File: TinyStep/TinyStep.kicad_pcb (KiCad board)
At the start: 2 copper layers, 17.8 x 25.4 mm, 2 parts, among them U1 ATtiny204-SS

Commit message: this might work
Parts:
- added A1: Pololu_Breakout_A4988, Module:Pololu_Breakout-16_15.2x20.3mm, F.Cu at (57.1, 35.5)
- added C2: 100uF 50V, Capacitor_THT:CP_Radial_D8.0mm_P3.50mm, F.Cu at (40.0, 39.6)
- added J1: Conn_01x03_Pin, Connector_PinHeader_2.54mm:PinHeader_1x03_P2.54mm_Vertical, F.Cu at (40.0, 52.1)
- added J2: Conn_01x04_Pin, Connector_JST:JST_XH_S4B-XH-A_1x04_P2.50mm_Horizontal, F.Cu at (52.0, 29.2)
- added J3: Conn_01x02_Pin, Connector_PinHeader_2.54mm:PinHeader_1x02_P2.54mm_Vertical, F.Cu at (57.8, 51.4)
- added J4: Conn_01x02_Pin, Connector_PinHeader_2.54mm:PinHeader_1x02_P2.54mm_Vertical, F.Cu at (57.8, 54.0)
- added J5: Conn_01x02_Pin, Connector_PinHeader_2.54mm:PinHeader_1x02_P2.54mm_Vertical, F.Cu at (57.8, 56.5)
- added J6: Conn_01x02_Pin, Connector_PinHeader_2.54mm:PinHeader_1x02_P2.54mm_Vertical, F.Cu at (57.8, 59.0)
- added J7: Barrel_Jack_Switch, Connector_BarrelJack:BarrelJack_Wuerth_6941xx301002, F.Cu at (47.9, 61.0)
- added R1: 10k, Resistor_SMD:R_0805_2012Metric_Pad1.20x1.40mm_HandSolder, B.Cu at (46.4, 45.1)
- added R2: 10k, Resistor_SMD:R_0805_2012Metric_Pad1.20x1.40mm_HandSolder, B.Cu at (44.5, 45.1)
- added R3: 10k, Resistor_SMD:R_0805_2012Metric_Pad1.20x1.40mm_HandSolder, B.Cu at (42.5, 45.1)
- added R4: 10k, Resistor_SMD:R_0805_2012Metric_Pad1.20x1.40mm_HandSolder, B.Cu at (51.4, 50.8)
- added R5: 10k, Resistor_SMD:R_0805_2012Metric_Pad1.20x1.40mm_HandSolder, B.Cu at (51.4, 52.7)
- added R6: 10k, Resistor_SMD:R_0805_2012Metric_Pad1.20x1.40mm_HandSolder, B.Cu at (51.4, 54.6)
- added R7: 10k, Resistor_SMD:R_0805_2012Metric_Pad1.20x1.40mm_HandSolder, B.Cu at (51.4, 56.5)
- added SW1: SW_DIP_x03, Button_Switch_SMD:SW_DIP_SPSTx03_Slide_Omron_A6S-310x_W8.9mm_P2.54mm, F.Cu at (47.6, 54.6)
- C1: value C -> 100n; footprint Capacitor_THT:C_Disc_D5.0mm_W2.5mm_P5.00mm -> Capacitor_SMD:C_0805_2012Metric_Pad1.18x1.45mm_HandSolder; moved to B.Cu
- U1: footprint BREAKOUT:DIP-16_SOIC_BREAKOUT -> Package_SO:SOIC-14_3.9x8.7mm_P1.27mm; moved to B.Cu
- moved U1 37.4 mm to (54.0, 42.5), turned to -90 degrees
- moved C1 29.1 mm to (48.3, 41.9), turned to 90 degrees
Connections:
- net Net-(U1-GND) renamed GND
- U1 pad 10: unconnected-(U1-~{RESET}/PA0-Pad10) -> UPDI
- U1 pad 11: unconnected-(U1-PA1-Pad11) -> A1_DI
- U1 pad 12: unconnected-(U1-PA2-Pad12) -> A1_ST
- U1 pad 13: unconnected-(U1-PA3-Pad13) -> A1_EN
- U1 pad 2: unconnected-(U1-PA4-Pad2) -> BTN0
- U1 pad 3: unconnected-(U1-PA5-Pad3) -> BTN1
- U1 pad 4: unconnected-(U1-PA6-Pad4) -> BTN3
- U1 pad 5: unconnected-(U1-PA7-Pad5) -> BTN2
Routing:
- net VCC: track 3.89 -> 55.4 mm
- net +12V: track 0.00 -> 36.9 mm
- net BTN3: track 0.00 -> 30.0 mm
- net UPDI: track 0.00 -> 28.1 mm, vias 0 -> 2
- net BTN2: track 0.00 -> 23.3 mm
- net BTN1: track 0.00 -> 21.3 mm, vias 0 -> 1
- net BTN0: track 0.00 -> 18.4 mm, vias 0 -> 1
- net A1_EN: track 0.00 -> 16.3 mm, vias 0 -> 1
- net Net-(A1-MS3): track 0.00 -> 14.8 mm
- net GND: track 10.4 -> 0.00 mm
- net Net-(A1-MS2): track 0.00 -> 10.3 mm
- net Net-(A1-MS1): track 0.00 -> 6.77 mm
- net Net-(A1-1B): track 0.00 -> 6.40 mm
- net Net-(A1-1A): track 0.00 -> 6.38 mm
- net Net-(A1-2A): track 0.00 -> 6.37 mm
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- added copper zone on B.Cu, net GND
- added copper zone on F.Cu, net GND
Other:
- board size 17.8 x 25.4 mm -> 26 x 54 mm
- board text added: "1 0"
- board text added: "B2 A2 A1 B1"
- board text added: "GND VCC UPDI"
- board text added: "MS1 MS2 MS3"

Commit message: v0.1
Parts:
- removed A1: Pololu_Breakout_A4988, Module:Pololu_Breakout-16_15.2x20.3mm
- removed the J3 at (57.8, 51.4)
- removed J6: Conn_01x02_Pin, Connector_PinHeader_2.54mm:PinHeader_1x02_P2.54mm_Vertical
- removed R5, R6, R7: 10k, Resistor_SMD:R_0805_2012Metric_Pad1.20x1.40mm_HandSolder
- removed SW1: SW_DIP_x03, Button_Switch_SMD:SW_DIP_SPSTx03_Slide_Omron_A6S-310x_W8.9mm_P2.54mm
- added A2: ~, Module_TMC2209_BTT:TMC2209_BTT, F.Cu at (52.2, 38.7)
- added C3: 10uF, Capacitor_SMD:C_0805_2012Metric_Pad1.18x1.45mm_HandSolder, B.Cu at (47.5, 41.2)
- added C4: 100nF, Capacitor_SMD:C_0805_2012Metric_Pad1.18x1.45mm_HandSolder, B.Cu at (49.7, 36.3)
- added C5: 22uF, Capacitor_SMD:C_0805_2012Metric_Pad1.18x1.45mm_HandSolder, B.Cu at (52.4, 40.3)
- added C6: 22uF, Capacitor_SMD:C_0805_2012Metric_Pad1.18x1.45mm_HandSolder, B.Cu at (50.4, 40.3)
- added JP1: SolderJumper_3_Bridged12, Jumper:SolderJumper-3_P1.3mm_Bridged12_RoundedPad1.0x1.5mm_NumberLabels, F.Cu at (53.6, 48.9)
- added JP2: SolderJumper_2_Open, Jumper:SolderJumper-2_P1.3mm_Open_RoundedPad1.0x1.5mm, F.Cu at (53.1, 51.8)
- added JP3: SolderJumper_2_Open, Jumper:SolderJumper-2_P1.3mm_Open_RoundedPad1.0x1.5mm, F.Cu at (50.5, 51.8)
- added JP4: SolderJumper_2_Open, Jumper:SolderJumper-2_P1.3mm_Open_RoundedPad1.0x1.5mm, F.Cu at (48.0, 51.8)
- added L1: 4.7uH, Inductor_SMD:L_0805_2012Metric_Pad1.15x1.40mm_HandSolder, B.Cu at (51.7, 36.3)
- added U2: AP63205WU, Package_TO_SOT_SMD:TSOT-23-6, B.Cu at (46.9, 38.0)
- C1: value 100n -> 100nF
- C2: value 100uF 50V -> 47uF 50V; footprint Capacitor_THT:CP_Radial_D8.0mm_P3.50mm -> Capacitor_SMD:CP_Elec_6.3x7.7
- J4: value Conn_01x02_Pin -> Conn_02x05_Odd_Even; footprint Connector_PinHeader_2.54mm:PinHeader_1x02_P2.54mm_Vertical -> Connector_PinHeader_2.54mm:PinHeader_2x05_P2.54mm_Vertical
- J5: value Conn_01x02_Pin -> Conn_02x02_Odd_Even; footprint Connector_PinHeader_2.54mm:PinHeader_1x02_P2.54mm_Vertical -> Connector_PinHeader_2.54mm:PinHeader_2x02_P2.54mm_Vertical
- R4: value 10k -> 1k
- moved R3 16.8 mm to (58.6, 40.3)
- moved J5 15.4 mm to (43.0, 60.8), turned to 0 degrees
- moved R2 13.0 mm to (56.6, 40.3)
- moved U1 11.1 mm to (50.7, 53.1), turned to 180 degrees
- moved C2 9.94 mm to (49.7, 37.6), turned to 0 degrees
- moved R1 9.44 mm to (54.5, 40.3)
- moved R4 7.95 mm to (57.7, 55.7), turned to 90 degrees
- moved J1 6.62 mm to (44.2, 57.2), turned to 180 degrees
- moved C1 6.10 mm to (50.7, 47.5), turned to 180 degrees
- moved J3 4.50 mm to (52.4, 60.4)
- moved J2 4.30 mm to (56.0, 27.7)
- moved J4 3.91 mm to (60.5, 51.2), turned to 0 degrees
- renumbered J7 to J3
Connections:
- C1 pad 1: GND -> VCC
- C1 pad 2: VCC -> GND
- J4 pad 1: BTN1 -> BTN0
- J4 pad 2: Net-(J4-Pin_2) -> GND
- J5 pad 1: BTN2 -> VCC
- J5 pad 2: Net-(J5-Pin_2) -> GND
- R3 pad 2: Net-(A1-MS1) -> A1_MS3_SW
- R4 pad 1: Net-(J3-Pin_2) -> /USART_Tx
- R4 pad 2: VCC -> A1_MS3_UART
- U1 pad 11: A1_DI -> BTN2
- U1 pad 12: A1_ST -> A1_DIAG
- U1 pad 2: BTN0 -> A1_ST
- U1 pad 3: BTN1 -> A1_DI
- U1 pad 4: BTN3 -> BTN0
- U1 pad 5: BTN2 -> BTN1
- U1 pad 6: unconnected-(U1-PB3-Pad6) -> A1_MS3_UART
- U1 pad 7: unconnected-(U1-PB2-Pad7) -> /USART_Tx
- U1 pad 8: unconnected-(U1-PB1-Pad8) -> BTN4
- U1 pad 9: unconnected-(U1-PB0-Pad9) -> BTN3
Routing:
- net +12V: track 36.9 -> 62.4 mm
- net UPDI: track 28.1 -> 5.84 mm, vias 2 -> 0
- net A1_MS3_SW: track 0.00 -> 22.3 mm, vias 0 -> 1
- net VCC: track 55.4 -> 73.3 mm, vias 0 -> 2
- net A1_DIAG: track 0.00 -> 16.6 mm
- net BTN3: track 30.0 -> 14.3 mm
- net BTN4: track 0.00 -> 14.1 mm
- net A1_MS3_UART: track 0.00 -> 13.6 mm, vias 0 -> 1
- net BTN1: track 21.3 -> 8.48 mm, vias 1 -> 0
- net BTN0: track 18.4 -> 8.65 mm, vias 1 -> 0
- net A1_EN: track 16.3 -> 8.52 mm, vias 1 -> 0
- net Net-(A2-MS2): track 10.3 -> 17.8 mm
- net BTN2: track 23.3 -> 16.4 mm
- net Net-(A1-MS1): track 6.77 -> 0.00 mm
- net A1_DI: track 6.15 -> 12.5 mm
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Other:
- outline, holes or cut-outs redrawn
- board text added: "MS3"
- board text added: "TinyStep v0.1"
- board text added: "UART"
- board text added: "VCC VIN"
- board text added: "sebastiangr.us"
- board text removed: "1 0"

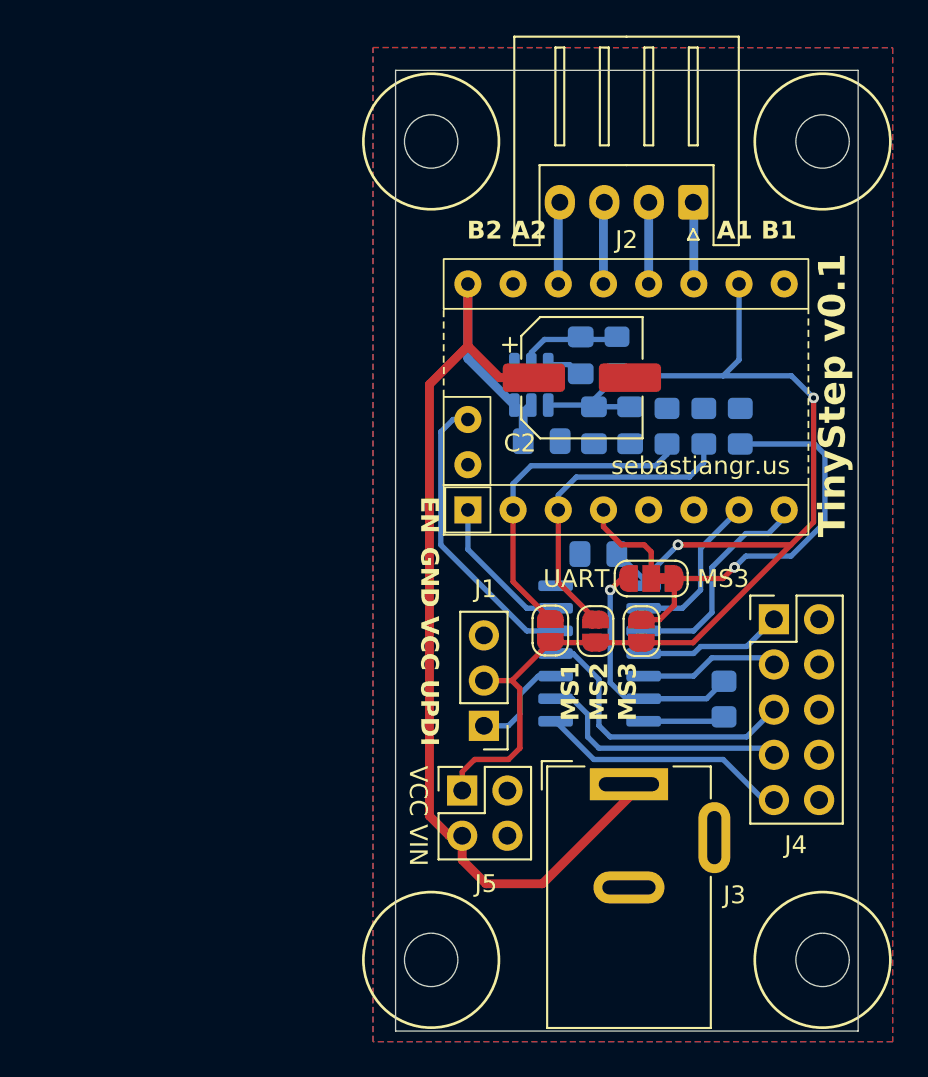
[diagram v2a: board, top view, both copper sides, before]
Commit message: GND vias, cleaner board
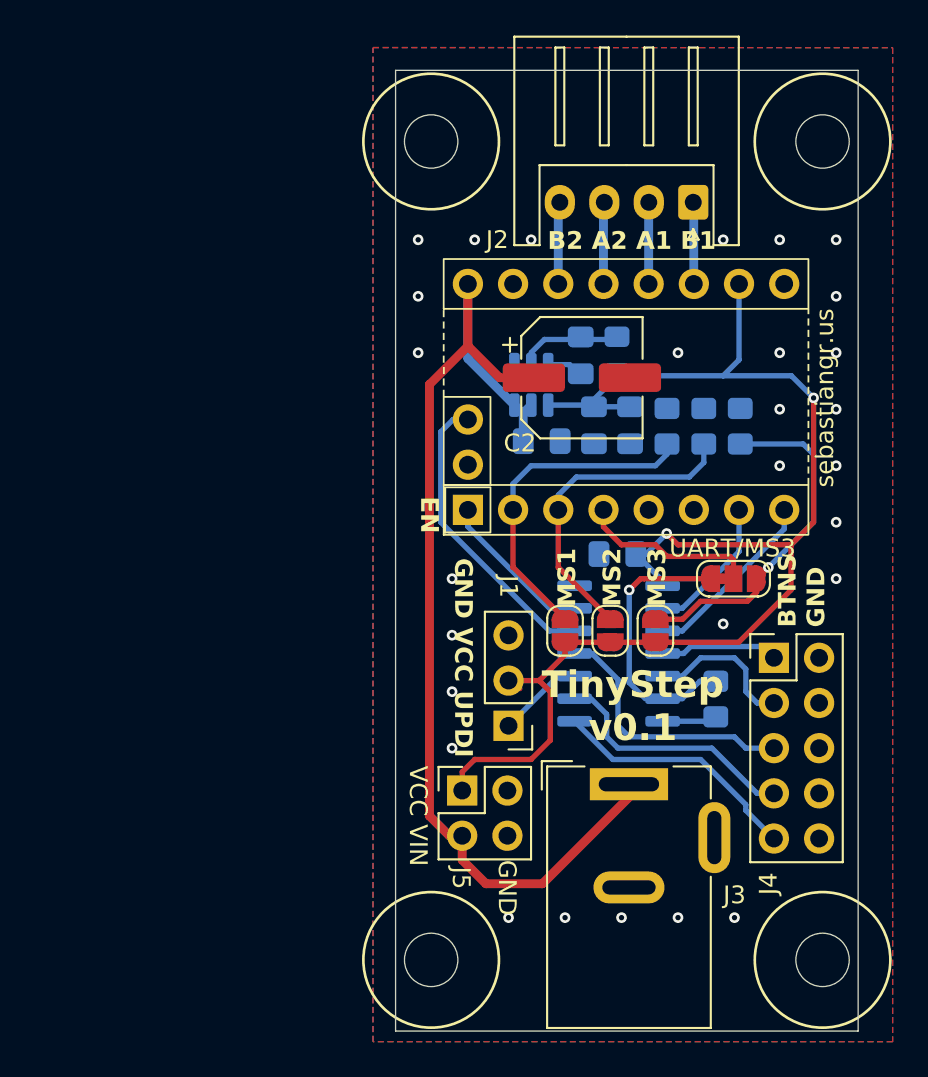
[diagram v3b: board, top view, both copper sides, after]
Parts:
- moved JP1 4.62 mm to (58.3, 48.9), turned to 0 degrees
- moved J4 2.17 mm to (60.5, 53.3)
- moved J1 1.38 mm to (45.6, 57.2)
- moved C1 1.07 mm to (51.7, 47.5)
- moved U1 1.07 mm to (51.8, 53.1)
- moved JP3 0.83 mm to (51.3, 51.8)
- moved JP4 0.83 mm to (48.8, 51.8)
- moved JP2 0.79 mm to (53.9, 51.8)
- moved R4 0.46 mm to (57.3, 55.7)
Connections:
- JP1 pad 1: A1_MS3_SW -> A1_MS3_UART
- JP1 pad 3: A1_MS3_UART -> A1_MS3_SW
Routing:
- net A1_MS3: track 5.71 -> 10.1 mm
- net VCC: track 73.3 -> 76.2 mm
- net A1_MS3_SW: track 22.3 -> 19.8 mm
- net A1_DI: track 12.5 -> 10.3 mm
- net /USART_Tx: track 4.62 -> 3.09 mm
- net A1_ST: track 9.47 -> 8.40 mm
- net A1_MS3_UART: track 13.6 -> 14.7 mm
- net UPDI: track 5.84 -> 4.87 mm
- net BTN2: track 16.4 -> 15.5 mm
- net BTN0: track 8.65 -> 7.78 mm
- net BTN3: track 14.3 -> 13.8 mm
- net GND: vias 0 -> 28
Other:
- board text added: "BTNS GND"
- board text added: "GND"
- board text added: "MS1"
- board text added: "MS2"
- board text added: "UART/MS3"
- board text removed: "MS1 MS2 MS3"
- board text removed: "UART"

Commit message: HT42B534 library
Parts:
- J4: value Conn_02x05_Odd_Even -> Conn_02x04_Odd_Even; footprint Connector_PinHeader_2.54mm:PinHeader_2x05_P2.54mm_Vertical -> Connector_PinHeader_2.54mm:PinHeader_2x04_P2.54mm_Vertical
- moved JP1 0.56 mm to (58.2, 48.3)
- moved J1 0.25 mm to (45.4, 57.1)
- moved J5 0.25 mm to (42.8, 61.0)
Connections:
- A2 pad 18: unconnected-(A2-INDEX-Pad18) -> A1_INDEX
- U1 pad 11: BTN2 -> A1_DIAG
- U1 pad 12: A1_DIAG -> A1_INDEX
- U1 pad 8: BTN4 -> BTN3
- U1 pad 9: BTN3 -> BTN2
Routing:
- net A1_INDEX: track 0.00 -> 16.0 mm
- net BTN4: track 14.1 -> 0.00 mm
- net VCC: track 76.2 -> 63.6 mm
- net A1_DIAG: track 16.9 -> 20.7 mm
- net BTN2: track 15.5 -> 12.4 mm
- net A1_MS3: track 10.1 -> 12.9 mm
- net +12V: track 62.4 -> 61.0 mm
- net BTN0: track 7.78 -> 6.68 mm
- net BTN3: track 13.8 -> 12.9 mm
- net UPDI: track 4.87 -> 5.71 mm
- net A1_MS3_UART: track 14.7 -> 15.5 mm
- net GND: vias 28 -> 33
- added copper zone on B.Cu, net +12V
- added copper zone on B.Cu, net VCC
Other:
- rule pad_to_mask_clearance: 0 -> 0.04
- board text added: "3 2 1 0"
- board text added: "BTN"
- board text added: "TinyStep v0.2"
- board text added: "UART MS3"
- board text removed: "BTNS GND"
- board text removed: "TinyStep v0.1"
- board text removed: "UART/MS3"
